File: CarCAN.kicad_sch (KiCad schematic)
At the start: 5 parts, among them IC1 TCAN337DCNR, U13 CDSOT23-T24CAN, U14 MCP2515-xST

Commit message: worked some more on converting components (unfinished)
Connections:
- net +3.3V: now also U14.18 (~{CS})
- net GND: now also U14.10 (VSS)
- net CAN_SPI_SCLK: now reaches U14.14 (SCK)
- net CAN_SPI_SI: now reaches U14.16 (SI)
- net CAN_SPI_SO: now reaches U14.17 (SO)
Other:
- moved on the sheet: U14

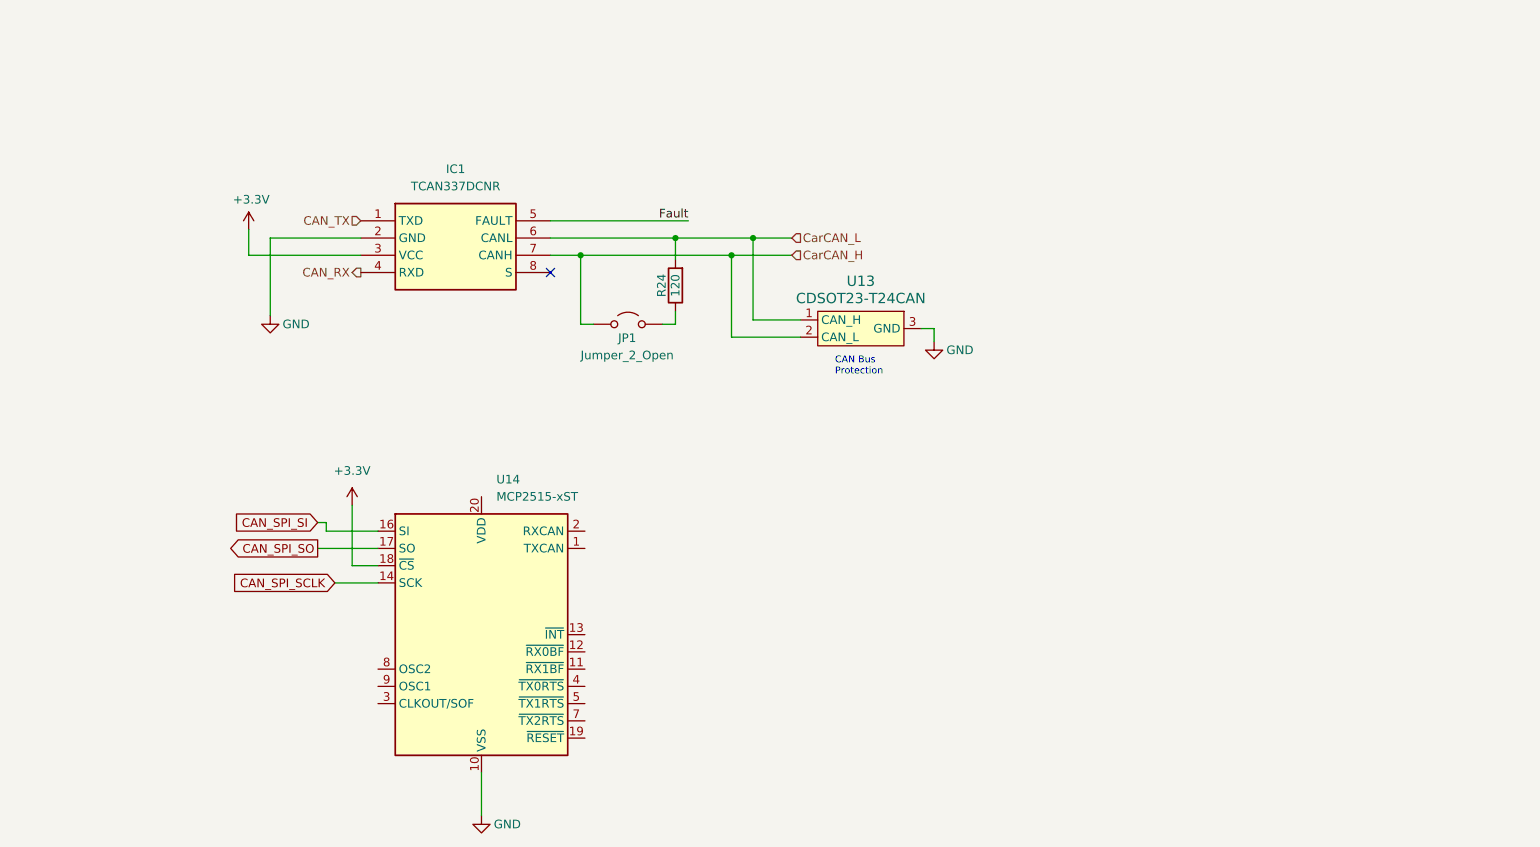
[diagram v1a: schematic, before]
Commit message: power dist, hdmi, and rtc are done; finding a new usb hub
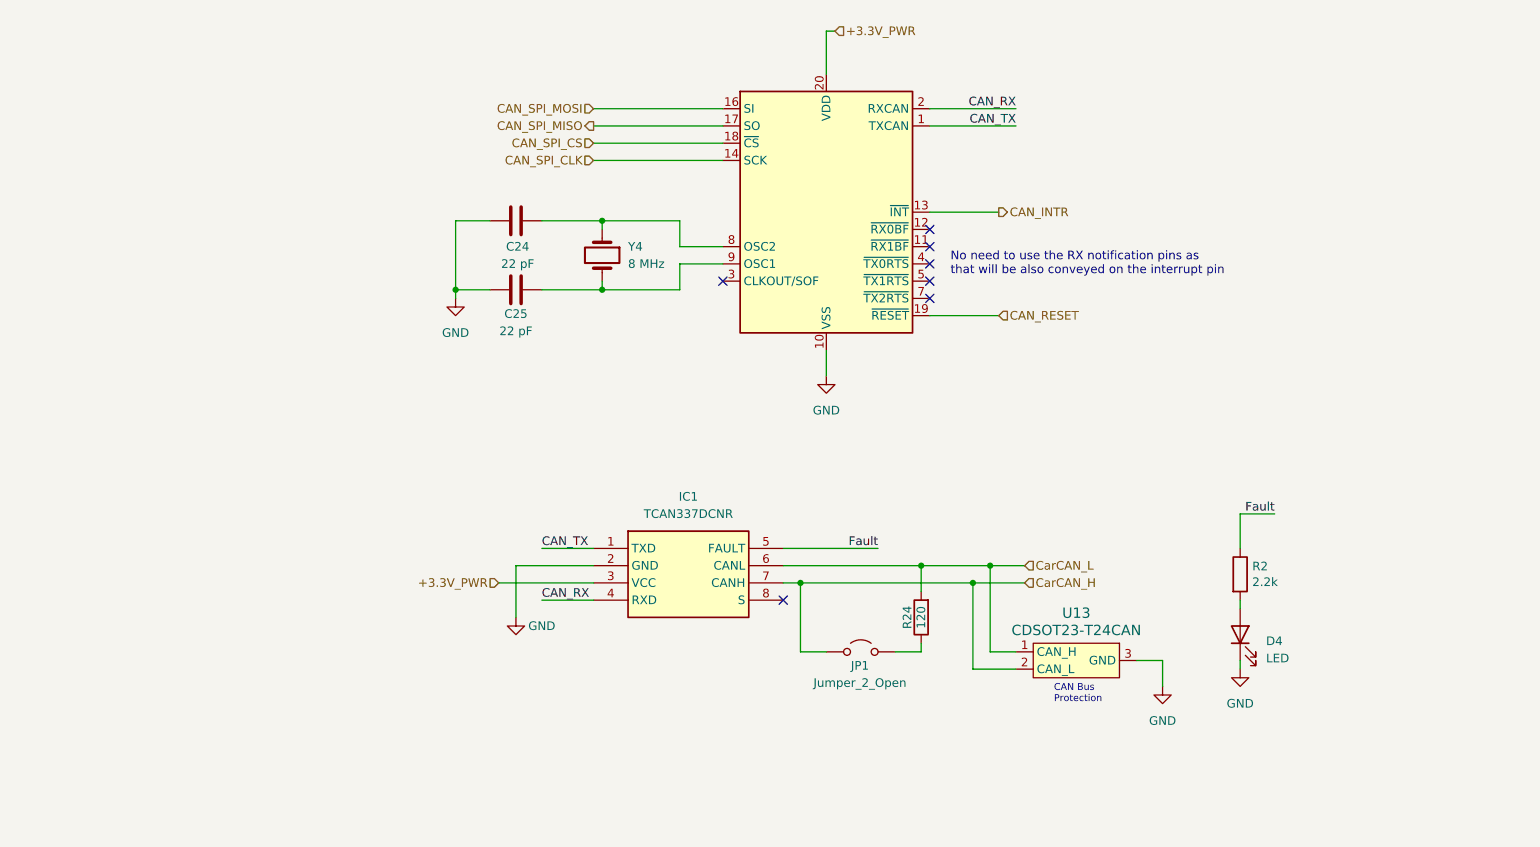
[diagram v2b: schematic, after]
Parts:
- added C24, C25: 22 pF, symbol Device:C
- added D4: LED, LED_SMD:LED_0805_2012Metric, symbol Device:LED
- added R2: 2.2k, Resistor_SMD:R_0805_2012Metric, symbol Device:R
- added Y4: 8 MHz, symbol Device:Crystal
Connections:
- net CAN_RX: now also U14.2 (RXCAN)
- net CAN_TX: now also U14.1 (TXCAN)
- net Fault: now also R2.1
- net GND: now also C24.1, C25.1, D4.1 (K)
- net CAN_INTR: now reaches U14.13 (~{INT})
- net CAN_RESET: now reaches U14.19 (~{RESET})
- net +3.3V_PWR: now reaches U14.20 (VDD)
- net +3.3V_PWR: now also IC1.3 (VCC)
- net at U14.8 (OSC2): now also C24.2, Y4.1
- net at U14.9 (OSC1): now also C25.2, Y4.2
- net +3.3V renamed CAN_SPI_CS
- net CAN_SPI_CS: no longer IC1.3 (VCC)
- net CAN_SPI_SCLK renamed CAN_SPI_CLK
- net CAN_SPI_SI renamed CAN_SPI_MOSI
- net CAN_SPI_SO renamed CAN_SPI_MISO
- new net: D4.2 (A), R2.2
- no-connect marks 1 -> 7
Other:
- note added: "No need to use the RX notification pins as that will be also conveyed on the interrupt pin"
- moved on the sheet: IC1, R24, U13

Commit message: finished USB i think, working on general gpio in more detail
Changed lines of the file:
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@@
 	(wire
 		(pts
-			(xy 214.63 110.49) (xy 214.63 115.57)
+			(xy 214.63 107.95) (xy 214.63 115.57)
 		)
 		(stroke
@@
 		(pts
 			(xy 107.95 118.11) (xy 119.38 118.11)
-		)
-		(stroke
-			(width 0)
-			(type default)
-		)
-	)
-	(wire
-		(pts
-			(xy 219.71 110.49) (xy 214.63 110.49)
 		)
 		(stroke
@@
 	)
 	(label "Fault"
-		(at 219.71 110.49 180)
+		(at 214.63 107.95 270)
 		(fields_autoplaced yes)
 		(effects
@@
 			)
 		)
-		(property "Datasheet" "http://ww1.microchip.com/downloads/en/DeviceDoc/21801e.pdf"
+		(property "Datasheet" "https://ww1.microchip.com/downloads/aemDocuments/documents/APID/ProductDocuments/DataSheets/MCP2515-Family-Data-Sheet-DS20001801K.pdf"
 			(at 156.21 86.36 0)
 			(effects

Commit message: random stuff before i screw with my windows install
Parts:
- added J2: CANConnector, UTSVT_Connectors:Molex_MicroFit3.0_1x4xP3.00mm_PolarizingPeg_Vertical, symbol utsvt-connectors:CANConnector
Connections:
- net CarCAN_H: no longer names the net of IC1.7 (CANH), JP1.1 (A), U13.2 (CAN_L)
- net CarCAN_H: now also J2.3 (CAN_H)
- net CarCAN_L: no longer names the net of IC1.6 (CANL), R24.2, U13.1 (CAN_H)
- net CarCAN_L: now also J2.4 (CAN_L)
- no-connect marks 7 -> 9
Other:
- moved on the sheet: C24, C25, D4, IC1, JP1, R2, R24, U13, Y4

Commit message: we ballin??
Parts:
- added C42: ~, symbol Device:C
- added D5: D, symbol Device:D
- added R25: R, symbol Device:R
- U14: value MCP2515-xST -> MCP2515-E/STVAO; Mouser link (none) -> https://www.mouser.com/ProductDetail/Microchip-Technology/M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
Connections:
- net CAN_RESET: now also D5.1 (K), R25.1; no longer U14.19 (~{RESET})
- net GND: now also C42.2
- new net: C42.1, D5.2 (A), R25.2, U14.19 (~{RESET})
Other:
- note added: "CAN Fault"
